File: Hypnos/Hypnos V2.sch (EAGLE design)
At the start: 25 parts

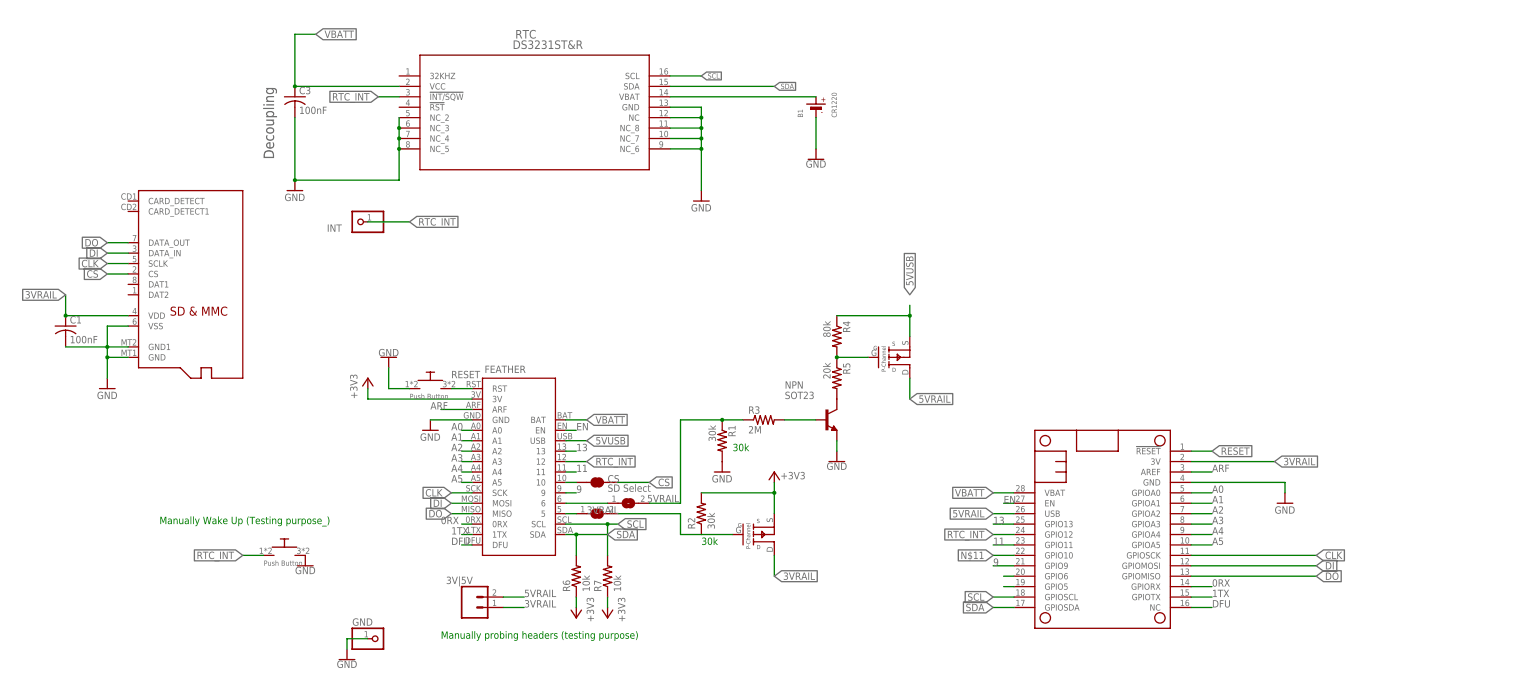
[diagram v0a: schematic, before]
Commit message: Testing for Version V2
Update from Version 1:
* 2 LEDs with current limiting resistors
* RTC is now powered from 3V3 instead of Vbat (using power from Vbat turns on Feather Battery Charger LED)
* Pull up resistor for SD chip select just like adalogger
* Rounded PCB corner
* Move the reset button to the middle of the board - mechanically more stable
* Add solder jumper for RTC-INT, normally connected

These LED has very high efficiency and only draw around 2mA instead of 20mA
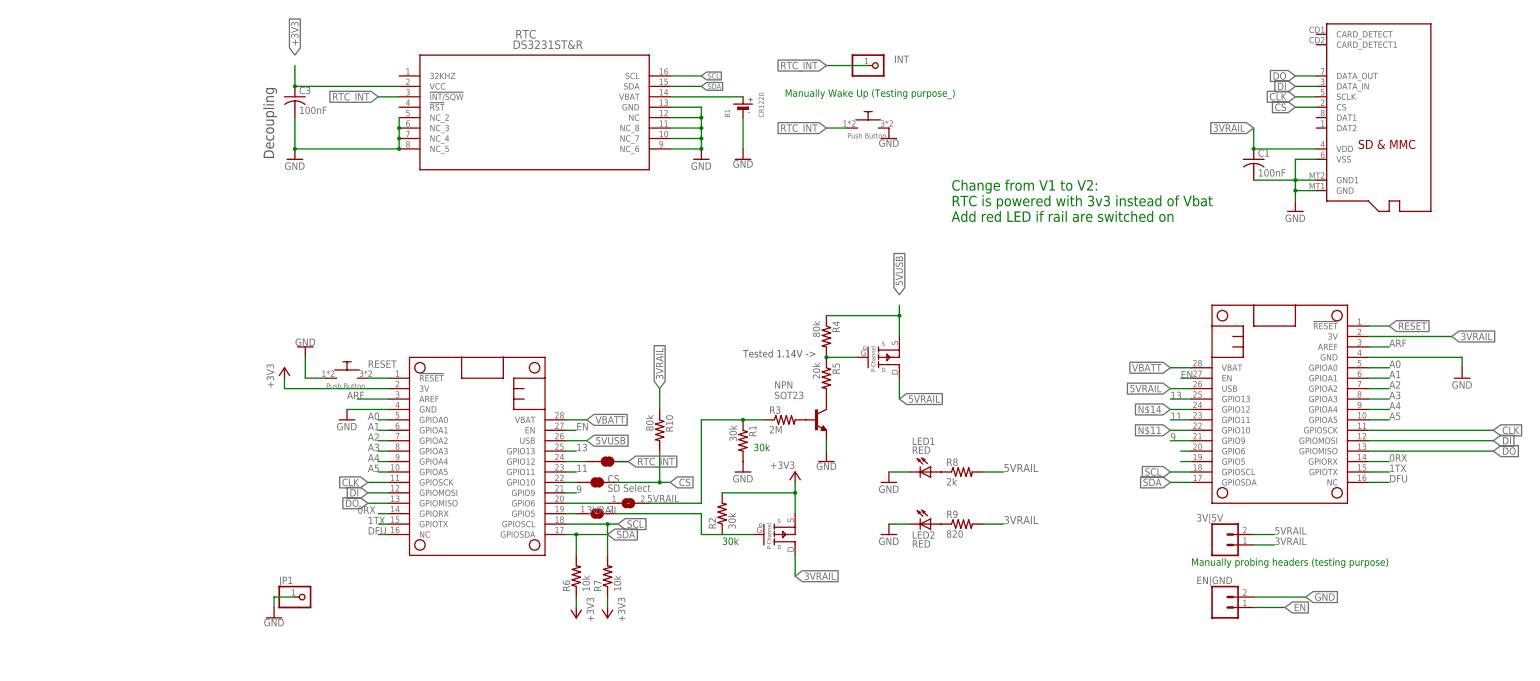
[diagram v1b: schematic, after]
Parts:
- removed FEATHER: BLUEFRUIT_M0, bluefruit_m0:BLUEFRUIT_M0
- removed GND: (no value), adafruitmodified:PINHD-1X1
- added EN|GND: (no value), SparkFun-Connectors:CONN_021X02_NO_SILK
- added JP1: (no value), adafruit:PINHD-1X1CB
- added LED1, LED2: RED, adafruit:LEDCHIPLED_0805
- added MS2: FEATHERWING, adafruit:FEATHERWING
- added R10: 80k, adafruit:R-US_R1206
- added R8: 2k, adafruit:R-US_R1206
- added R9: 820, adafruit:R-US_R1206
- added RTC_INT: JUMPER-SMT_2_NC_TRACE_SILK, SparkFun-Jumpers:JUMPER-SMT_2_NC_TRACE_SILK
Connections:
- new net N$12: LED1.A, R8.1
- new net N$13: LED2.A, R9.1
- new net N$14: MS1.GPIO12, MS2.GPIO12, RTC_INT.1
- net +3V3: now also C3.1, MS2.3V, RTC.VCC; no longer FEATHER.3V
- net 0RX: now also MS2.GPIORX; no longer FEATHER.0RX
- net 11: now also MS2.GPIO11; no longer FEATHER.11
- net 13: now also MS2.GPIO13; no longer FEATHER.13
- net 1TX: now also MS2.GPIOTX; no longer FEATHER.1TX
- net 3VRAIL: now also R10.1, R9.2
- net 5VRAIL: now also R8.2
- net 5VUSB: now also MS2.USB; no longer FEATHER.USB
- net 9: now also MS2.GPIO9; no longer FEATHER.9
- net A0: now also MS2.GPIOA0; no longer FEATHER.A0
- net A1: now also MS2.GPIOA1; no longer FEATHER.A1
- net A2: now also MS2.GPIOA2; no longer FEATHER.A2
- net A3: now also MS2.GPIOA3; no longer FEATHER.A3
- net A4: now also MS2.GPIOA4; no longer FEATHER.A4
- net A5: now also MS2.GPIOA5; no longer FEATHER.A5
- net ARF: now also MS2.AREF; no longer FEATHER.ARF
- net CLK: now also MS2.GPIOSCK; no longer FEATHER.SCK
- net CS: now also R10.2
- net DFU: now also MS2.NC; no longer FEATHER.DFU
- net DI: now also MS2.GPIOMOSI; no longer FEATHER.MOSI
- net DO: now also MS2.GPIOMISO; no longer FEATHER.MISO
- net EN: now also EN|GND.1, MS2.EN; no longer FEATHER.EN
- net GND: now also EN|GND.2, JP1.1, LED1.C, LED2.C, MS2.GND; no longer FEATHER.GND, GND.1
- net N$1: now also MS2.GPIO6; no longer FEATHER.6
- net N$11: now also MS2.GPIO10; no longer FEATHER.10
- net N$3: now also MS2.GPIO5; no longer FEATHER.5
- net RESET: now also MS2.!RESET; no longer FEATHER.RST
- net RTC_INT: now also RTC_INT.2; no longer FEATHER.12, MS1.GPIO12
- net SCL: now also MS2.GPIOSCL; no longer FEATHER.SCL
- net SDA: now also MS2.GPIOSDA; no longer FEATHER.SDA
- net VBATT: now also MS2.VBAT; no longer C3.1, FEATHER.BAT, RTC.VCC
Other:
- note added: "Change from V1 to V2: RTC is powered with 3v3 instead of Vbat Add red LED if rail are switched on"
- note added: "Tested 1.14V ->"
- moved on the sheet: 3V|5V, B1, C1, INT, NPN, R1, R2, R3, R4, R5

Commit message: Schematic Change for Hypnos V2
Update Hypnos V2
* Change from BJT to Logic MOSFET. Using BJT require current limiting resistor and also involve more calculation.
* Remove R5 to simplify the circuit
* Increase trace width for all power rail
* Change resistors footprint to get more space and better indication for solder orientation

Update eDNA.lbr
* Add mosfet footprints
* Other footprints for power control related project

Update ReadMe
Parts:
- removed NPN: SOT23, transistor:BC849
- removed R3: 2M, adafruit:R-US_R1206
- removed R5: 20k, adafruit:R-US_R1206
- added C2: 100pF, resistor:C-USC0805
- added U$3: NMOS, eDNA:NMOS
- C1, C3: device adafruit:C-USC1206 -> resistor:C-USC1206
- R1, R10, R2, R6, R7: device adafruit:R-US_R1206 -> Resistor_Capacitor:WSLP1206R0500FEA
- R4: value 80k -> 100k; device adafruit:R-US_R1206 -> Resistor_Capacitor:WSLP1206R0500FEA
- R8: value 2k -> 6.2k; device adafruit:R-US_R1206 -> Resistor_Capacitor:WSLP1206R0500FEA
- R9: value 820 -> 3k; device adafruit:R-US_R1206 -> Resistor_Capacitor:WSLP1206R0500FEA
- renumbered EN|GND to GND|EN
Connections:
- removed net N$6: NPN.B, R3.2
- removed net N$9: NPN.C, R5.2
- net GND: now also C2.2, U$3.S; no longer NPN.E
- net N$10: now also C2.1, U$3.D; no longer R5.1
- net N$4: now also U$3.G; no longer R3.1
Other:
- note added: "Voltage drop: 1.8V Should drive at 0.5mA"
- note removed: "Tested 1.14V ->"
- moved on the sheet: R1

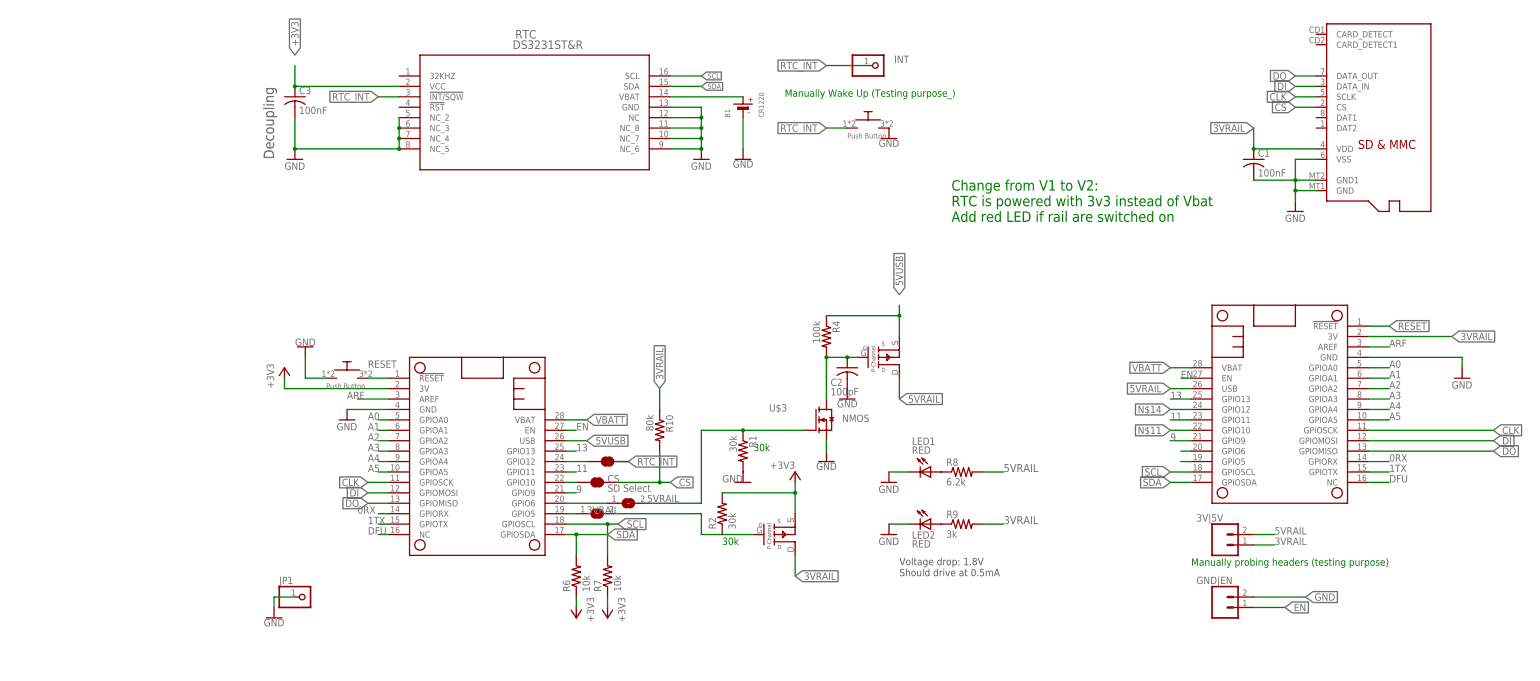
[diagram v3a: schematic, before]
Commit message: Added Diode
Hardware fix for uSD card current leak. Added diode with low current leakage to prevent current from SPI pins going back to 3VRAIL.
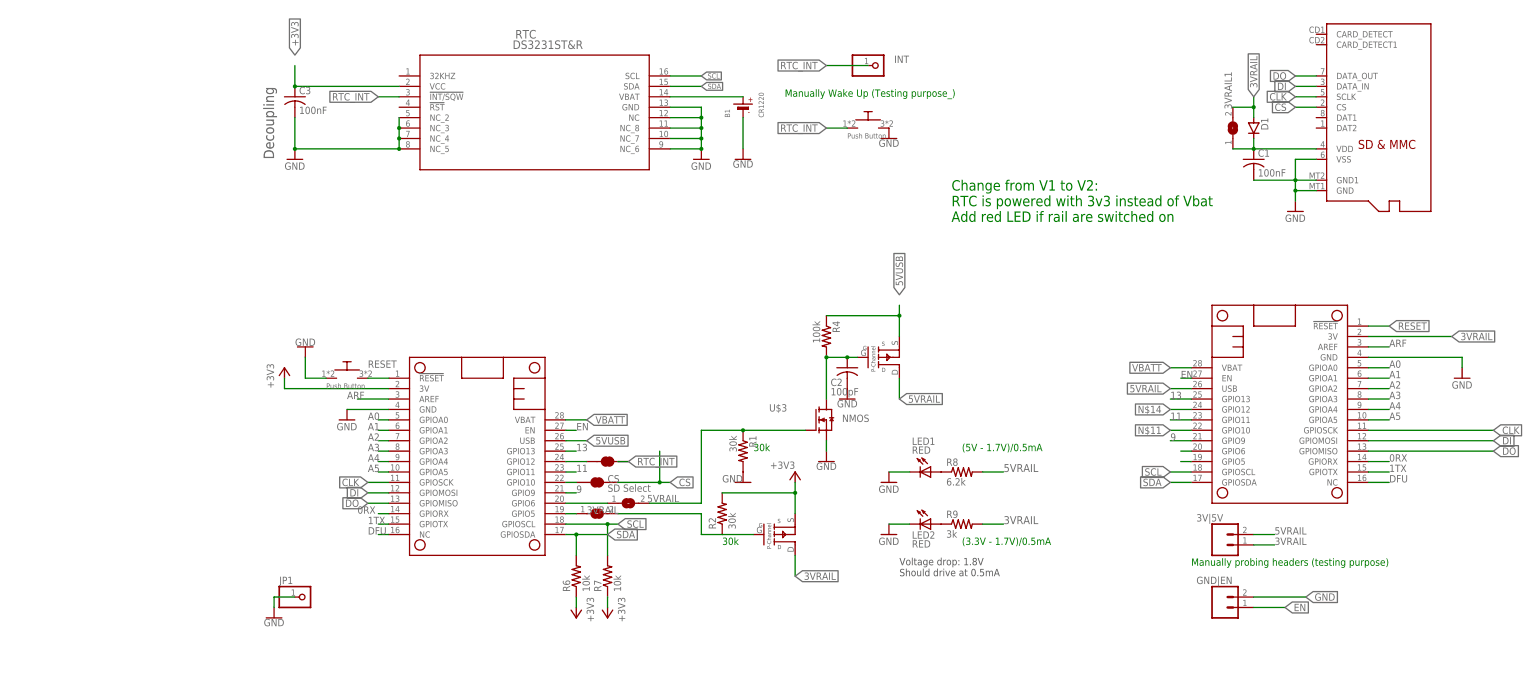
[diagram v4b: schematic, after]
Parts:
- removed R10: 80k, Resistor_Capacitor:WSLP1206R0500FEA
- added 3VRAIL1: (no value), jumper:SJ
- added D1: (no value), semicon-smd-ipc:D-SOD123
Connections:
- new net VDD: 3VRAIL1.1, C1.1, D1.C, MICROSD.VDD
- net 3VRAIL: now also 3VRAIL1.2, D1.A; no longer C1.1, MICROSD.VDD, R10.1
- net CS: no longer R10.2
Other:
- note added: "(3.3V - 1.7V)/0.5mA"
- note added: "(5V - 1.7V)/0.5mA"
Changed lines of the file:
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@@
 <part name="GND11" library="supply1" library_urn="urn:adsk.eagle:library:371" deviceset="GND" device=""/>
 <part name="MS2" library="adafruit" deviceset="FEATHERWING" device="" package3d_urn="urn:adsk.eagle:package:6240959/1"/>
-<part name="R10" library="Resistor_Capacitor" library_urn="urn:adsk.eagle:library:11396451" deviceset="WSLP1206R0500FEA" device="" package3d_urn="urn:adsk.eagle:package:10872898/2" value="80k"/>
 <part name="RTC_INT" library="SparkFun-Jumpers" library_urn="urn:adsk.eagle:library:528" deviceset="JUMPER-SMT_2_NC_TRACE" device="_SILK" package3d_urn="urn:adsk.eagle:package:39281/1" value=""/>
 <part name="GND|EN" library="SparkFun-Connectors" library_urn="urn:adsk.eagle:library:513" deviceset="CONN_02" device="1X02_NO_SILK" package3d_urn="urn:adsk.eagle:package:38051/1"/>
@@
 <part name="C2" library="resistor" library_urn="urn:adsk.eagle:library:348" deviceset="C-US" device="C0805" package3d_urn="urn:adsk.eagle:package:23617/2" value="100pF"/>
 <part name="GND12" library="SparkFun-PowerSymbols" library_urn="urn:adsk.eagle:library:530" deviceset="GND" device=""/>
+<part name="D1" library="semicon-smd-ipc" library_urn="urn:adsk.eagle:library:353" deviceset="D-" device="SOD123" package3d_urn="urn:adsk.eagle:package:26308/2"/>
+<part name="3VRAIL1" library="jumper" library_urn="urn:adsk.eagle:library:252" deviceset="SJ" device="" package3d_urn="urn:adsk.eagle:package:15471/1"/>
 </parts>
 <sheets>
@@
 <text x="756.92" y="-665.48" size="1.778" layer="97">Voltage drop: 1.8V
 Should drive at 0.5mA</text>
+<text x="772.16" y="-635" size="1.778" layer="91">(5V - 1.7V)/0.5mA</text>
+<text x="772.16" y="-657.86" size="1.778" layer="91">(3.3V - 1.7V)/0.5mA</text>
 </plain>
 <instances>
@@
 </instance>
 <instance part="MS2" gate="G$1" x="637.54" y="-612.14" smashed="yes" rot="R270" grouprefs="MOSFET_CIRCUITRY"/>
-<instance part="R10" gate="G$1" x="698.5" y="-629.92" smashed="yes" rot="R270" grouprefs="MOSFET_CIRCUITRY">
-<attribute name="NAME" x="699.9986" y="-626.11" size="1.778" layer="95" rot="R270"/>
-<attribute name="VALUE" x="695.198" y="-626.11" size="1.778" layer="96" rot="R270"/>
-</instance>
 <instance part="RTC_INT" gate="G$1" x="685.8" y="-637.54" smashed="yes" grouprefs="MOSFET_CIRCUITRY">
 <attribute name="VALUE" x="688.34" y="-638.048" size="1.778" layer="96" font="vector" align="top-left"/>
@@
 <instance part="GND12" gate="1" x="744.22" y="-622.3" smashed="yes">
 <attribute name="VALUE" x="744.22" y="-622.554" size="1.778" layer="96" align="top-center"/>
+</instance>
+<instance part="D1" gate="G$1" x="843.28" y="-556.26" smashed="yes" rot="R270" grouprefs="SDCARD">
+<attribute name="NAME" x="845.058" y="-553.72" size="1.778" layer="95" rot="R270"/>
+<attribute name="VALUE" x="839.597" y="-553.72" size="1.778" layer="96" rot="R270"/>
+</instance>
+<instance part="3VRAIL1" gate="1" x="838.2" y="-556.26" smashed="yes" rot="R90">
+<attribute name="NAME" x="837.946" y="-551.688" size="1.778" layer="95" rot="R90"/>
+<attribute name="VALUE" x="842.01" y="-558.8" size="1.778" layer="96" rot="R90"/>
 </instance>
 </instances>
@@
 <wire x1="688.34" y1="-642.62" x2="698.5" y2="-642.62" width="0.1524" layer="91" grouprefs="MOSFET_CIRCUITRY"/>
 <label x="701.04" y="-642.62" size="1.778" layer="95" xref="yes" grouprefs="MOSFET_CIRCUITRY"/>
-<pinref part="R10" gate="G$1" pin="2"/>
 <wire x1="698.5" y1="-642.62" x2="701.04" y2="-642.62" width="0.1524" layer="91" grouprefs="MOSFET_CIRCUITRY"/>
 <wire x1="698.5" y1="-635" x2="698.5" y2="-642.62" width="0.1524" layer="91" grouprefs="MOSFET_CIRCUITRY"/>
@@
 </segment>
 <segment>
-<wire x1="843.28" y1="-561.34" x2="843.28" y2="-556.26" width="0.1524" layer="91" grouprefs="SDCARD"/>
-<pinref part="MICROSD" gate="G$1" pin="VDD"/>
-<label x="843.28" y="-556.26" size="1.778" layer="95" rot="R180" xref="yes" grouprefs="SDCARD"/>
-<pinref part="C1" gate="G$1" pin="1"/>
-<wire x1="843.28" y1="-561.34" x2="858.52" y2="-561.34" width="0.1524" layer="91" grouprefs="SDCARD"/>
-<junction x="843.28" y="-561.34" grouprefs="SDCARD"/>
-</segment>
-<segment>
 <pinref part="R9" gate="G$1" pin="2"/>
 <wire x1="777.24" y1="-652.78" x2="782.32" y2="-652.78" width="0.1524" layer="91" grouprefs="MOSFET_CIRCUITRY"/>
@@
 </segment>
 <segment>
-<pinref part="R10" gate="G$1" pin="1"/>
-<wire x1="698.5" y1="-624.84" x2="698.5" y2="-619.76" width="0.1524" layer="91" grouprefs="MOSFET_CIRCUITRY"/>
-<label x="698.5" y="-619.76" size="1.778" layer="95" rot="R90" xref="yes" grouprefs="MOSFET_CIRCUITRY"/>
+<pinref part="D1" gate="G$1" pin="A"/>
+<wire x1="843.28" y1="-553.72" x2="843.28" y2="-551.18" width="0.1524" layer="91" grouprefs="SDCARD"/>
+<label x="843.28" y="-548.64" size="1.778" layer="95" rot="R90" xref="yes" grouprefs="SDCARD"/>
+<wire x1="843.28" y1="-551.18" x2="843.28" y2="-548.64" width="0.1524" layer="91" grouprefs="SDCARD"/>
+<wire x1="838.2" y1="-551.18" x2="843.28" y2="-551.18" width="0.1524" layer="91" grouprefs="SDCARD"/>
+<junction x="843.28" y="-551.18" grouprefs="SDCARD"/>
+<pinref part="3VRAIL1" gate="1" pin="2"/>
 </segment>
 </net>
@@
 </segment>
 </net>
+<net name="VDD" class="0">
+<segment>
+<pinref part="C1" gate="G$1" pin="1"/>
+<pinref part="MICROSD" gate="G$1" pin="VDD"/>
+<wire x1="843.28" y1="-561.34" x2="858.52" y2="-561.34" width="0.1524" layer="91" grouprefs="SDCARD"/>
+<pinref part="D1" gate="G$1" pin="C"/>
+<wire x1="843.28" y1="-561.34" x2="843.28" y2="-558.8" width="0.1524" layer="91" grouprefs="SDCARD"/>
+<junction x="843.28" y="-561.34" grouprefs="SDCARD"/>
+<wire x1="838.2" y1="-561.34" x2="843.28" y2="-561.34" width="0.1524" layer="91" grouprefs="SDCARD"/>
+<pinref part="3VRAIL1" gate="1" pin="1"/>
+</segment>
+</net>
